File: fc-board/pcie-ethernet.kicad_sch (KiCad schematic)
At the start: 53 parts, among them J16 Conn_01x04_Pin, U11 LAN7430T-I/Y9X, Y1 DSC1001CI2-025.0000T

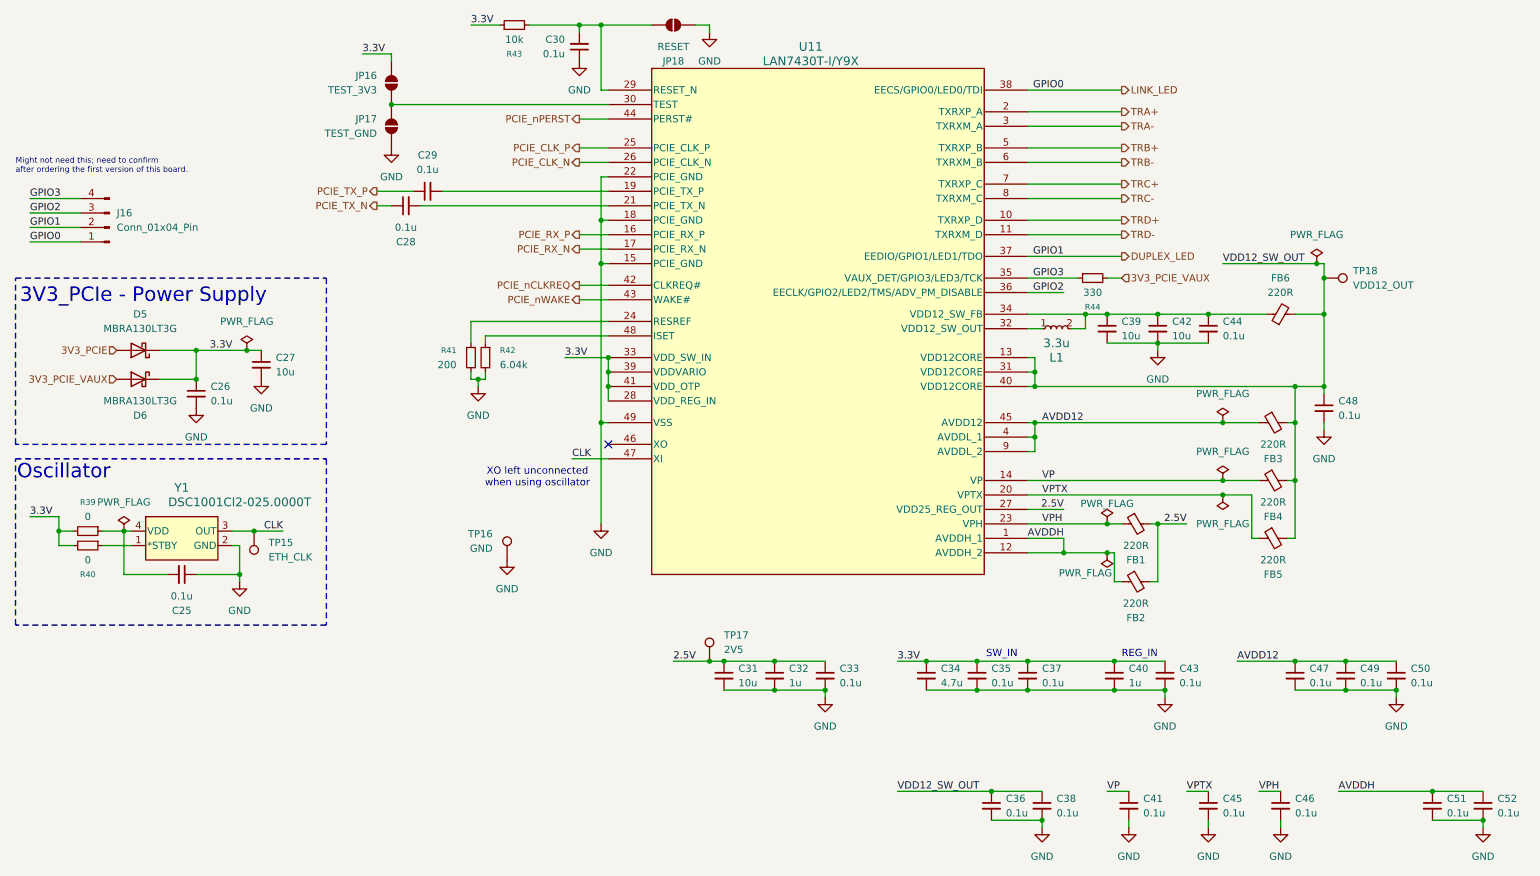
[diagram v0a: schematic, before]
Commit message: Fixed incorrect routes, modified gondola eth, cosmetics
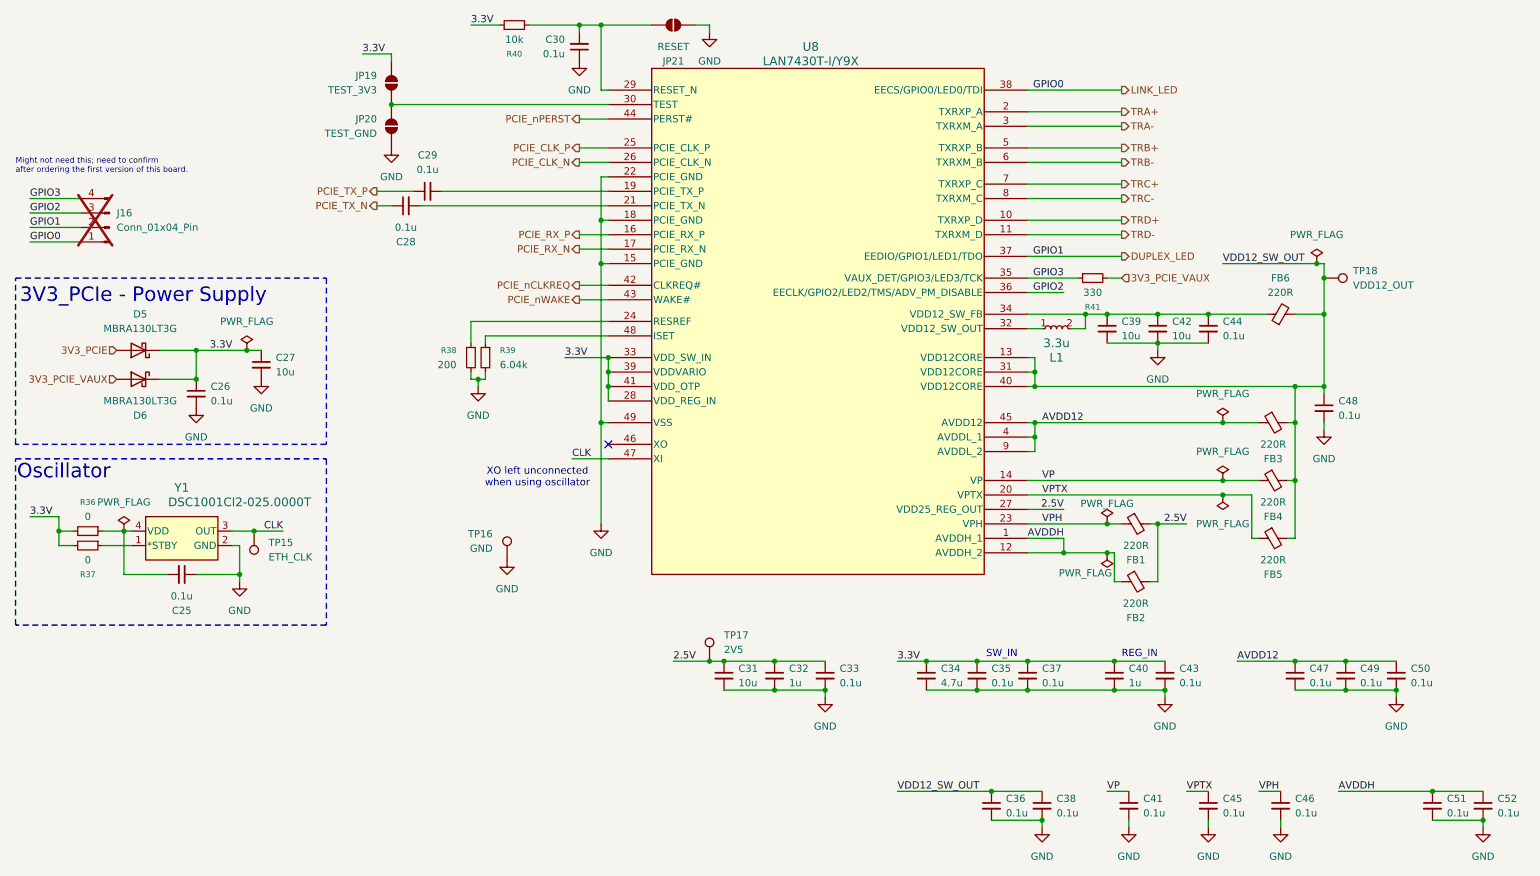
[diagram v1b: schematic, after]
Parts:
- J16: now not fitted
- renumbered JP16 to JP19, JP17 to JP20, JP18 to JP21, R39 to R36, R40 to R37, R41 to R38, R42 to R39, R43 to R40, R44 to R41, U11 to U8

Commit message: Fixed PCIe routing, voltage sensing, added DAQ toggle, LCT interrupt, bias sensing resistors, SD card, and more
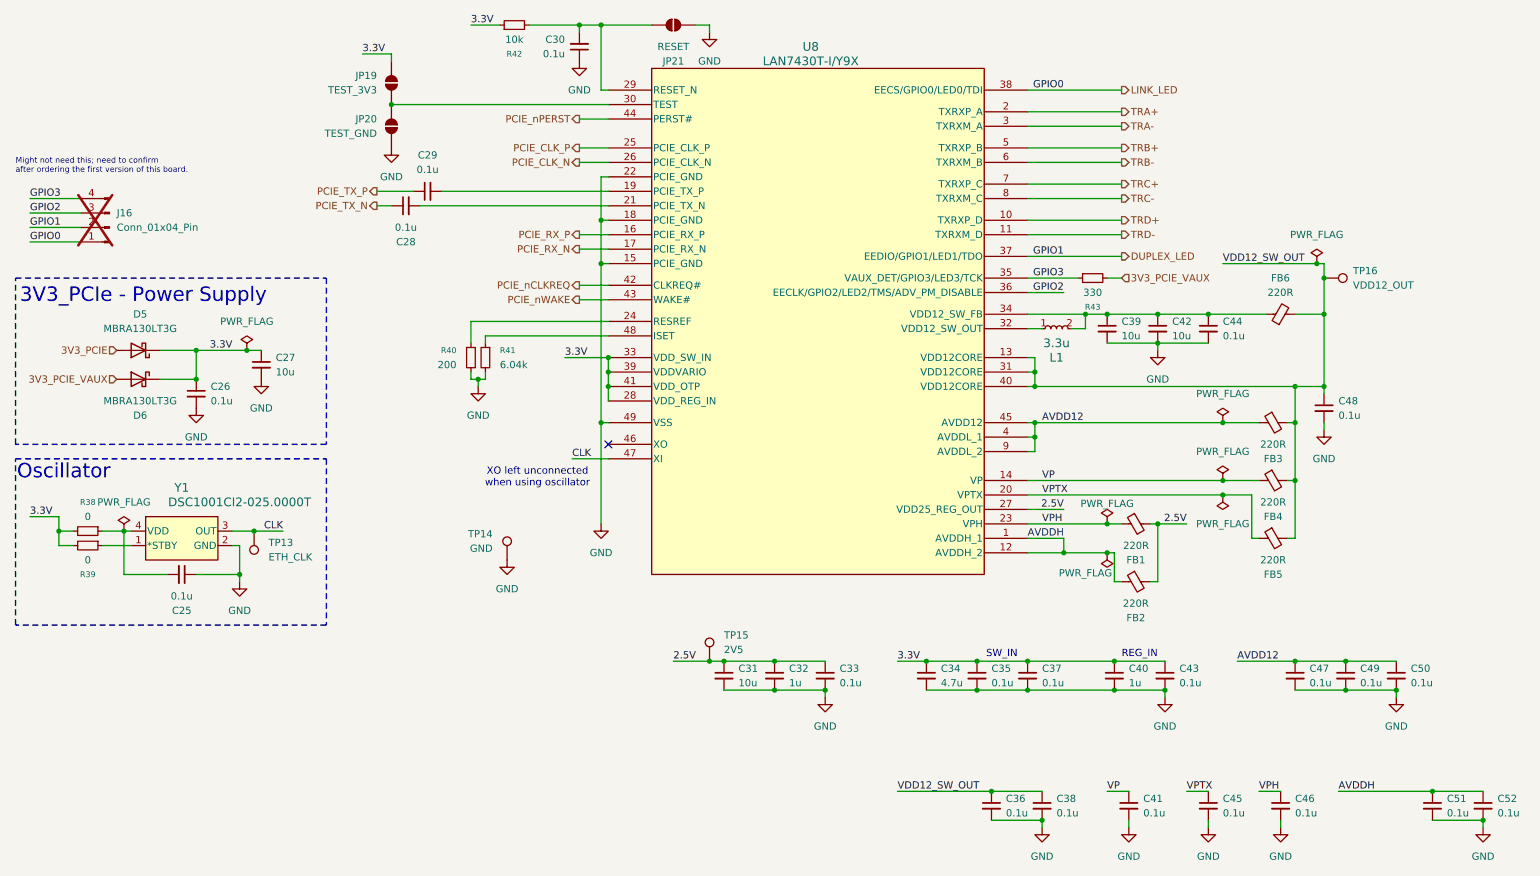
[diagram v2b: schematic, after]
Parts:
- renumbered R36 to R38, R37 to R39, R38 to R40, R39 to R41, R40 to R42, R41 to R43, TP15 to TP13, TP16 to TP14, TP17 to TP15, TP18 to TP16
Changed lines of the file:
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@@
 		(dnp no)
 		(fields_autoplaced yes)
-		(property "Reference" "R36"
+		(property "Reference" "R38"
 			(at 27.94 100.33 90)
 			(effects
@@
 			(project "fc-board"
 				(path "/14bbabed-904f-4efc-8ba4-be00e59385c4/edd7e4f6-7524-424d-ae74-0eda33819a09/39ada011-5e2b-4e01-950b-3cc6cc5801c0"
-					(reference "R36")
+					(reference "R38")
 					(unit 1)
 				)
@@
 		(on_board yes)
 		(dnp no)
-		(property "Reference" "R39"
+		(property "Reference" "R41"
 			(at 100.33 73.6599 0)
 			(effects
@@
 			(project "fc-board"
 				(path "/14bbabed-904f-4efc-8ba4-be00e59385c4/edd7e4f6-7524-424d-ae74-0eda33819a09/39ada011-5e2b-4e01-950b-3cc6cc5801c0"
-					(reference "R39")
+					(reference "R41")
 					(unit 1)
 				)
@@
 		(on_board yes)
 		(dnp no)
-		(property "Reference" "R38"
+		(property "Reference" "R40"
 			(at 92.71 73.6599 0)
 			(effects
@@
 			(project ""
 				(path "/14bbabed-904f-4efc-8ba4-be00e59385c4/edd7e4f6-7524-424d-ae74-0eda33819a09/39ada011-5e2b-4e01-950b-3cc6cc5801c0"
-					(reference "R38")
+					(reference "R40")
 					(unit 1)
 				)
@@
 		(on_board yes)
 		(dnp no)
-		(property "Reference" "TP16"
+		(property "Reference" "TP14"
 			(at 99.06 105.9179 0)
 			(effects
@@
 			(project ""
 				(path "/14bbabed-904f-4efc-8ba4-be00e59385c4/edd7e4f6-7524-424d-ae74-0eda33819a09/39ada011-5e2b-4e01-950b-3cc6cc5801c0"
-					(reference "TP16")
+					(reference "TP14")
 					(unit 1)
 				)
@@
 		(dnp no)
 		(fields_autoplaced yes)
-		(property "Reference" "TP17"
+		(property "Reference" "TP15"
 			(at 139.7 123.6979 0)
 			(effects
@@
 			(project ""
 				(path "/14bbabed-904f-4efc-8ba4-be00e59385c4/edd7e4f6-7524-424d-ae74-0eda33819a09/39ada011-5e2b-4e01-950b-3cc6cc5801c0"
-					(reference "TP17")
+					(reference "TP15")
 					(unit 1)
 				)
@@
 		(on_board yes)
 		(dnp no)
-		(property "Reference" "R41"
+		(property "Reference" "R43"
 			(at 204.47 66.04 90)
 			(effects
@@
 			(project ""
 				(path "/14bbabed-904f-4efc-8ba4-be00e59385c4/edd7e4f6-7524-424d-ae74-0eda33819a09/39ada011-5e2b-4e01-950b-3cc6cc5801c0"
-					(reference "R41")
+					(reference "R43")
 					(unit 1)
 				)
@@
 		(dnp no)
 		(fields_autoplaced yes)
-		(property "Reference" "R37"
+		(property "Reference" "R39"
 			(at 27.94 113.03 90)
 			(effects
@@
 			(project ""
 				(path "/14bbabed-904f-4efc-8ba4-be00e59385c4/edd7e4f6-7524-424d-ae74-0eda33819a09/39ada011-5e2b-4e01-950b-3cc6cc5801c0"
-					(reference "R37")
+					(reference "R39")
 					(unit 1)
 				)
@@
 		(on_board yes)
 		(dnp no)
-		(property "Reference" "R40"
+		(property "Reference" "R42"
 			(at 102.87 21.59 90)
 			(effects
@@
 			(project ""
 				(path "/14bbabed-904f-4efc-8ba4-be00e59385c4/edd7e4f6-7524-424d-ae74-0eda33819a09/39ada011-5e2b-4e01-950b-3cc6cc5801c0"
-					(reference "R40")
+					(reference "R42")
 					(unit 1)
 				)
@@
 		(dnp no)
 		(fields_autoplaced yes)
-		(property "Reference" "TP15"
+		(property "Reference" "TP13"
 			(at 59.69 107.4419 0)
 			(effects
@@
 			(project ""
 				(path "/14bbabed-904f-4efc-8ba4-be00e59385c4/edd7e4f6-7524-424d-ae74-0eda33819a09/39ada011-5e2b-4e01-950b-3cc6cc5801c0"
-					(reference "TP15")
+					(reference "TP13")
 					(unit 1)
 				)
@@
 		(dnp no)
 		(fields_autoplaced yes)
-		(property "Reference" "TP18"
+		(property "Reference" "TP16"
 			(at 250.19 59.6899 90)
 			(effects
@@
 			(project ""
 				(path "/14bbabed-904f-4efc-8ba4-be00e59385c4/edd7e4f6-7524-424d-ae74-0eda33819a09/39ada011-5e2b-4e01-950b-3cc6cc5801c0"
-					(reference "TP18")
+					(reference "TP16")
 					(unit 1)
 				)

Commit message: Fleshed out part numbers and design rules
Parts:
- TP13, TP14, TP15, TP16: symbol Connector:TestPoint -> fc-board:TestPoint; now left out of the parts list
